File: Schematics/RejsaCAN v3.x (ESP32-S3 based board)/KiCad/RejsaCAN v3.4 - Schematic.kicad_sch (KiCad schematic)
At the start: 75 parts, among them J1 Micro-Fit 3.0 4P R/A, J2 U.FL, Q1 SS8050, U1 ESP32-S3-WROOM-1(N16R8), U2 SN65HVD230DR, U3 ME2807A33M3G, U4 LMR14006XDDCR, U5 MT9700, U6 CPC1018N, U7 LG290P03AAMD

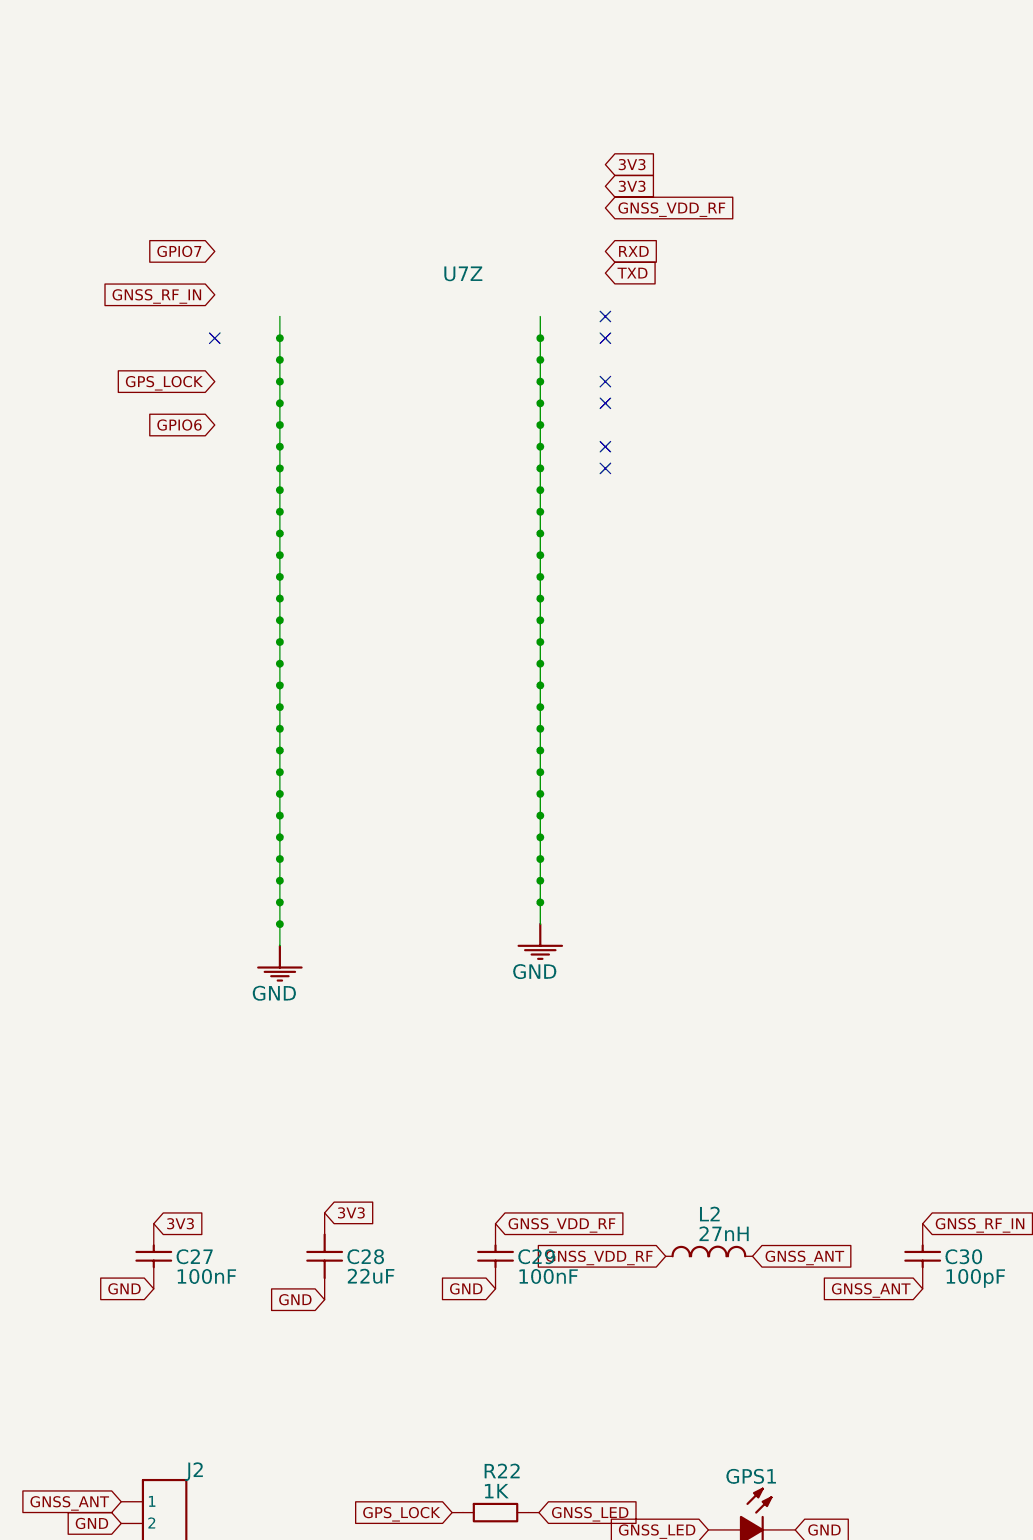
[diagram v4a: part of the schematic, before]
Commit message: Correct the GNSS front end against Quectel's reference circuit
The bias tee and decoupling were provisional standard values. Checked
against LG290P(03) Hardware Design V1.1 section 5.2 / Figure 17 and
corrected to match it component-for-component.

  L2   27nH -> 68nH   Quectel: "at least 68 nH". 27nH gave only ~200
                      ohm of isolation at the bottom of the L5/B2a band
  R23  10R  new       series in VDD_RF; Quectel's stated protection for
                      an active antenna shorted to the ground plane
  C31  100pF new      bias-node bypass, pairs with C29 100nF per Fig.17
  C32  33pF  new      completes the 22uF/100nF/33pF VCC network; the
                      smallest value must sit closest to pin 23
  D13  TVS   new      antenna ESD, Cj <= 0.6 pF as specified
  FB1  ferrite new    see below

VCC now arrives as GNSS_VCC through FB1 rather than straight off 3V3.
Quectel explicitly advises against powering this module from a
switching converter and asks for <50 mV ripple, but the only rail on
this board is the LMR14006 buck. A ferrite pi filter is a compromise,
not compliance -- a dedicated LDO for the module is the correct fix and
is left as an open decision.

Verified against the netlist:
  VDD_RF -R23- GNSS_BIAS -L2- GNSS_ANT -C30- GNSS_RF_IN
  GNSS_BIAS carries C29 + C31; GNSS_ANT carries J2 and D13.

Two firmware constraints this imposes, neither of which is visible in
the netlist:
  - RESET_N has an internal 20k pull-up and Quectel prohibits an
    external one. GPIO7 must be configured open-drain, never push-pull.
  - RTK_STAT is high at startup, so GPS1 is lit before the first fix.
    ANT_ON on that pin is documented as not yet implemented.

D13 and FB1 carry placeholder values and need real part numbers before
fabrication.

Co-Authored-By: Claude Opus 5 <noreply@anthropic.com>
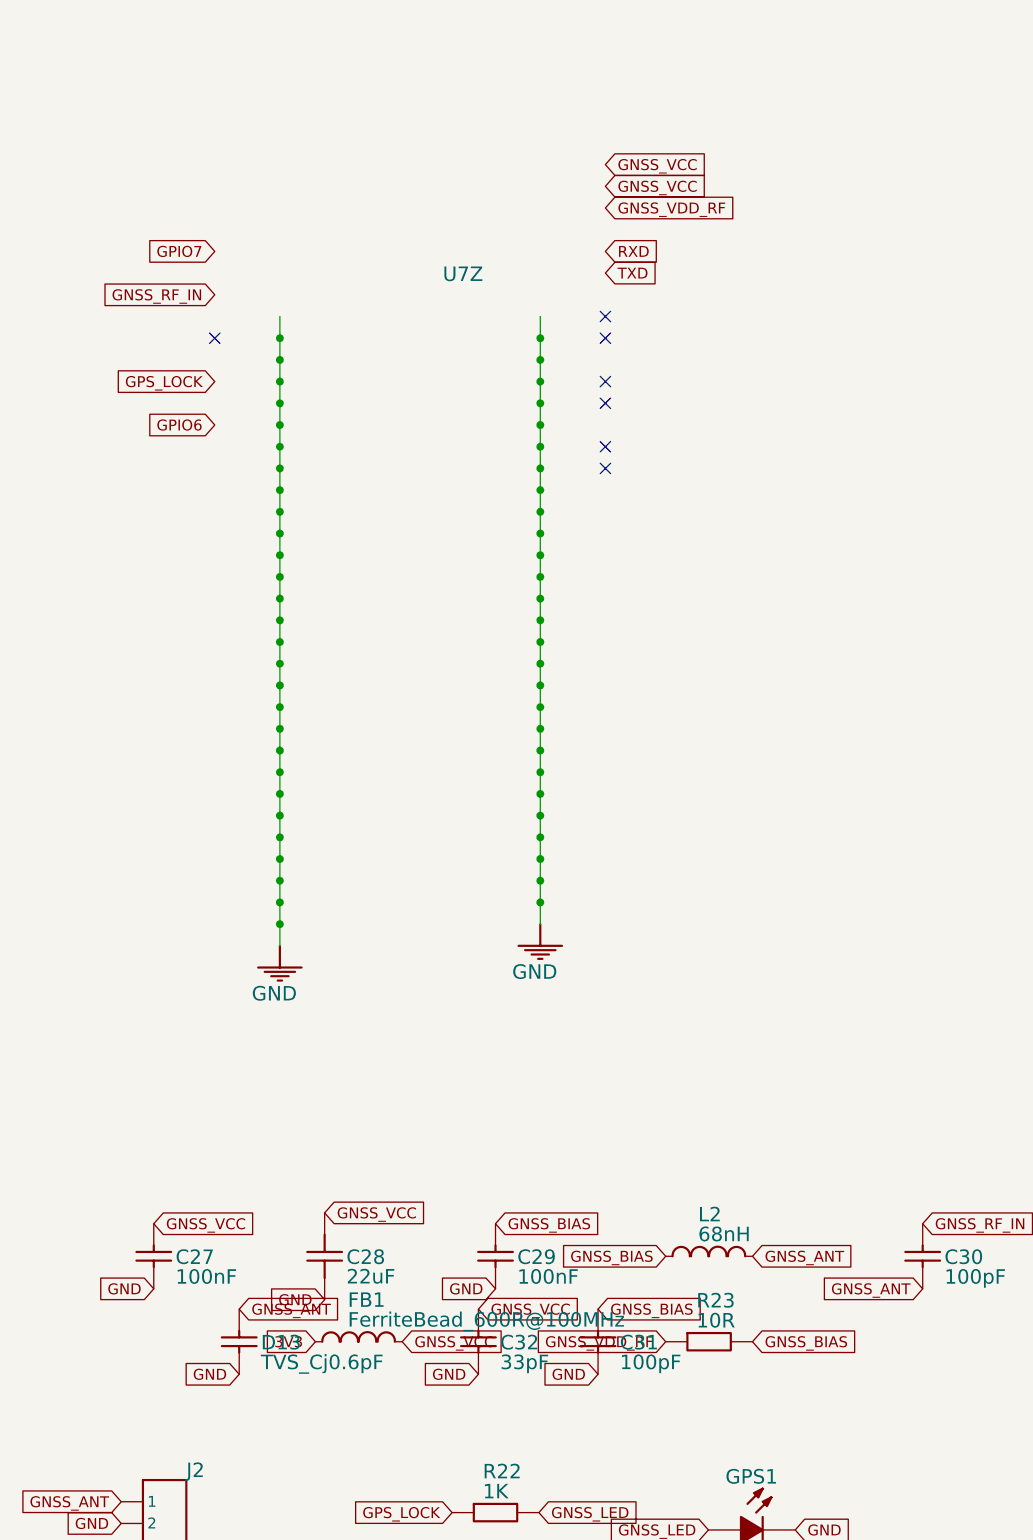
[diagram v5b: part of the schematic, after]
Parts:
- added C31: 100pF, Capacitor_SMD:C_0402_1005Metric, symbol CL05B104KO5NNNC_1
- added C32: 33pF, Capacitor_SMD:C_0402_1005Metric, symbol CL05B104KO5NNNC_1
- added D13: TVS_Cj0.6pF, Diode_SMD:D_0402_1005Metric, symbol CL05B104KO5NNNC_1
- added FB1: FerriteBead_600R@100MHz, Inductor_SMD:L_0402_1005Metric, symbol SLP6028S100MTT
- added R23: 10R, Resistor_SMD:R_0402_1005Metric, symbol 0402WGF1001TCE
- L2: value 27nH -> 68nH
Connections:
- net 3V3: now also FB1.1; no longer C27.2, C28.2
- net GND: now also C31.1, C32.1, D13.1
- net GNSS_ANT: now also D13.2
- net GNSS_VDD_RF: now also R23.1; no longer C29.2, L2.1
- new net GNSS_BIAS: C29.2, C31.2, L2.1, R23.2
- new net GNSS_VCC: C27.2, C28.2, C32.2, FB1.2

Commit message: Uprate the 3V3 supply for the GNSS load; retarget the photorelay
Adding the LG290P pushed the 3V3 rail past its regulator. Measured
against datasheets rather than estimated:

  ESP32-S3 802.11b TX @20.5dBm   355 mA   DS v1.8 T6-4
  LG290P acquisition and tracking 135 mA  HW Design Table 11
  active antenna LNA via VDD_RF    30 mA
  SN65HVD230 dominant, 60R         70 mA  SLOS346O
  microSD write                   150 mA
  LEDs + photorelay + MT9700 Iq      8 mA
                                  -------
  peak                            748 mA

U4 (LMR14006) is a 600 mA part, so peak sat at 125% of rating.
Pre-GNSS the same sum was 583 mA -- the original board was already
just under the line, and the GNSS block is exactly what consumed the
remaining headroom. Continuous is ~282 mA, which was never the problem.

  U4  LMR14006XDDCR -> LMR14010ADDCR   600 mA -> 1 A
  L1  10uH -> 15uH

LMR14010A is a genuine drop-in: same DDC/TSOT-6 land, same pin order
(CB/GND/FB/SHDN/VIN/SW), same 0.765 V reference, so R9 33k / R10 10k
still set 3.29 V and C7, D5 and the output caps are unchanged.

It also fixes a latent bug that predates this work. The LMR14006X
switches at 2.1 MHz with a 95 ns minimum on-time, i.e. a 20% minimum
duty cycle, so it can only hold 3.3 V up to Vin ~16.5 V -- on a board
upstream rates for 5-24 V. At 24 V the required on-time is 65 ns, below
the minimum, forcing pulse-skipping. LMR14010A runs at 700 kHz, a 6.65%
minimum duty, good past 50 V. The 15uH also matters at the new
frequency: TI's K_IND=0.3 rule needs >=13.6uH, so 10uH was under the
minimum and would have run 36-43% ripple.

  U6  CPC1018N -> GAQY212GS
  R20 500 -> 390

CPC1018N tube stock at LCSC is zero and the reel is $3.96. GAQY212GS is
the same SOP-4 1-Form-A AC/DC land and better on every axis -- 0.6R vs
0.8R, 0.8A vs 0.6A, 2500V vs 1500V isolation, 83k in stock at $0.60.
Its recommended I_F window starts at 5 mA, so R20 goes to 390R for
5.4 mA; that is still comfortably above the 1 mA guara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
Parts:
- L1: value 10uH -> 15uH; Supplier Part C254862 -> (none)
- R20: value 500 -> 390; Supplier Part C25117 -> (none)
- U4: value LMR14006XDDCR -> LMR14010ADDCR; Supplier Part C478074 -> (none)
- U6: value CPC1018N -> GAQY212GS
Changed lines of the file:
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@@
 			)
 		)
-		(property "Value" "LMR14006XDDCR"
+		(property "Value" "LMR14010ADDCR"
 			(at 94.107 155.3591 0)
 			(show_name no)
@@
 			)
 		)
-		(property "Supplier Part" "C478074"
+		(property "Supplier Part" ""
 			(at 102.87 162.56 0)
 			(hide yes)
@@
 			)
 		)
-		(property "Value" "10uH"
+		(property "Value" "15uH"
 			(at 135.8646 169.1767 0)
 			(show_name no)
@@
 			)
 		)
-		(property "Supplier Part" "C254862"
+		(property "Supplier Part" ""
 			(at 137.16 172.72 0)
 			(hide yes)
@@
 			)
 		)
-		(property "Value" "CPC1018N"
+		(property "Value" "GAQY212GS"
 			(at 225.831 31.8389 0)
 			(hide yes)
@@
 			)
 		)
-		(property "Value" "500"
+		(property "Value" "390"
 			(at 211.861 34.6583 0)
 			(show_name no)
@@
 			)
 		)
-		(property "Supplier Part" "C25117"
+		(property "Supplier Part" ""
 			(at 213.36 38.1 0)
 			(hide yes)
